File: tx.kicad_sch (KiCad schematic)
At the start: 58 parts, among them Q301 MMBF170, Q302 MMBF170, Q303 MMBF170, Q304 MMBF170, Q305 MMBF170, Q306 MMBF170, Q307 MMBF170, Q308 MMBF170, Q309 MMBF170, Q310 MMBF170, Q311 MMBF170, Q312 MMBF170, T301 BN-43-202_DualPri_CTSec, U301 ICE40UP5K-SG48ITR, U302 CD74ACT541SM96, U303 TLV70012

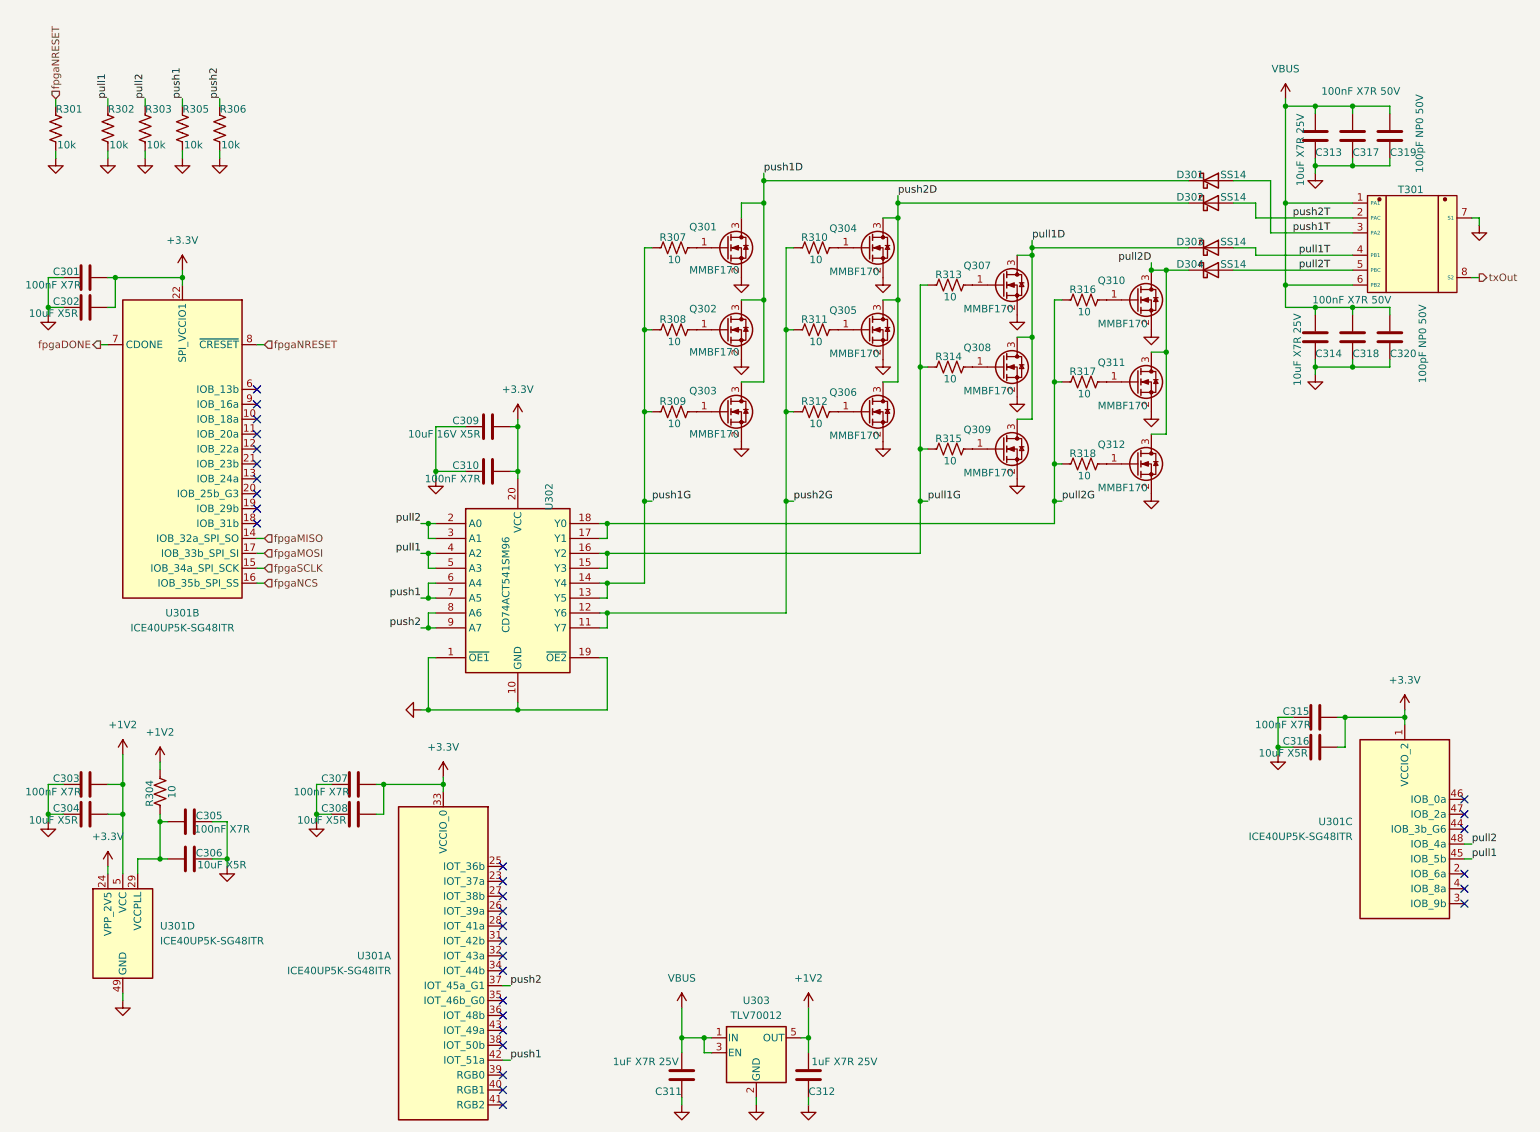
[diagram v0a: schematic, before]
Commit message: Tarted up, 3d models applied, better footprints and BOM, ready to submit for PCBA
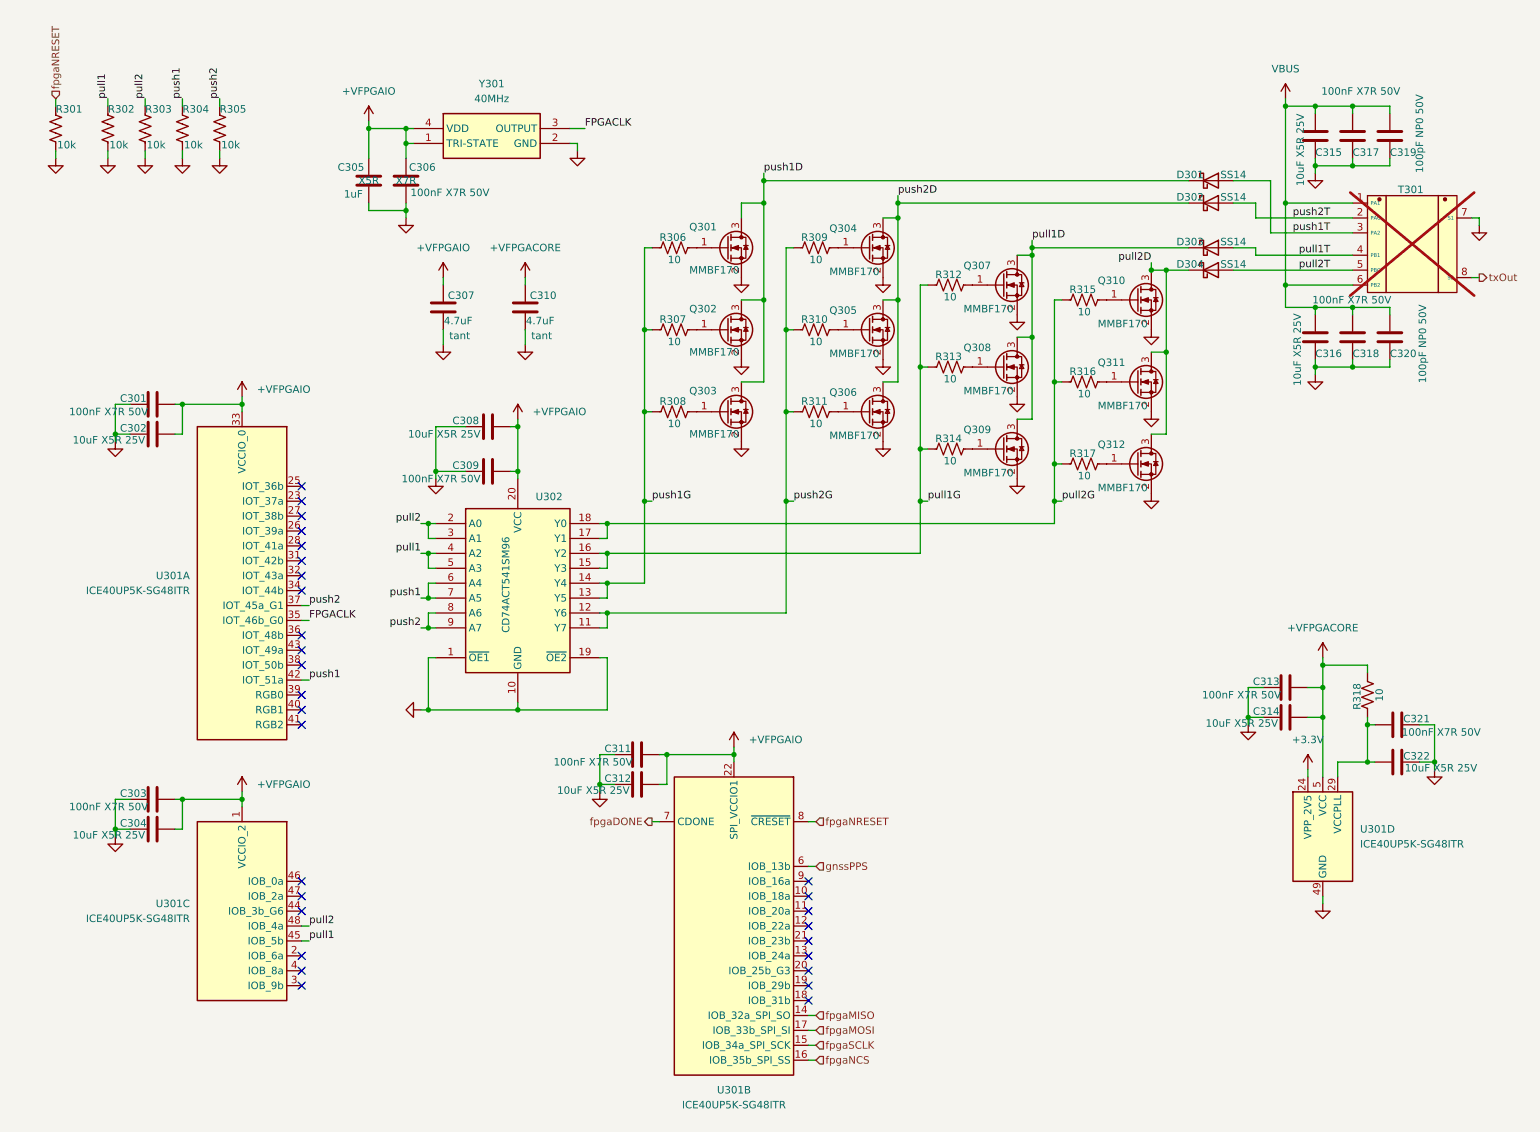
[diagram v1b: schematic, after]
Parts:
- removed C311, C312: 1uF X7R 25V, Capacitor_SMD:C_0603_1608Metric, symbol Device:C
- removed U303: TLV70012, Package_TO_SOT_SMD:SOT-353_SC-70-5, symbol Regulator_Linear:TLV70012_SOT353
- added C305: 1uF, Capacitor_SMD:C_0402_1005Metric, symbol Device:C
- added C306: 100nF X7R 50V, Capacitor_SMD:C_0603_1608Metric, symbol Device:C
- added C307, C310: 4.7uF, Capacitor_SMD:C_0402_1005Metric, symbol Device:C
- added Y301: 40MHz, Library:ECSTXO201633400TR, symbol Library:ECS-TXO-2016-33-400-TR
- C301: renamed from C307; value 100nF X7R -> 100nF X7R 50V; LCSC C14663 -> C24452
- C302: renamed from C308; value 10uF X5R -> 10uF X5R 25V; LCSC C19702 -> C96446
- C303: renamed from C315; value 100nF X7R -> 100nF X7R 50V; LCSC C14663 -> C24452
- C304: renamed from C316; value 10uF X5R -> 10uF X5R 25V; LCSC C19702 -> C96446
- C308: renamed from C309; value 10uF 16V X5R -> 10uF X5R 25V; footprint Capacitor_SMD:C_0805_2012Metric -> Capacitor_SMD:C_0603_1608Metric; LCSC C1713 -> C96446
- C309: renamed from C310; value 100nF X7R -> 100nF X7R 50V; LCSC C14663 -> C24452
- C311: renamed from C301; value 100nF X7R -> 100nF X7R 50V; LCSC C14663 -> C24452
- C312: renamed from C302; value 10uF X5R -> 10uF X5R 25V; LCSC C19702 -> C96446
- C313: renamed from C303; value 100nF X7R -> 100nF X7R 50V; LCSC C14663 -> C24452
- C314: renamed from C304; value 10uF X5R -> 10uF X5R 25V; LCSC C19702 -> C96446
- C315: renamed from C313; value 10uF X7R 25V -> 10uF X5R 25V
- C316: renamed from C314; value 10uF X7R 25V -> 10uF X5R 25V
- C317, C318: LCSC C14663 -> C24452
- C319, C320: footprint Capacitor_SMD:C_0603_1608Metric -> Capacitor_SMD:C_0402_1005Metric; LCSC C14665 -> C106200
- C321: renamed from C305; value 100nF X7R -> 100nF X7R 50V; LCSC C14663 -> C24452
- C322: renamed from C306; value 10uF X5R -> 10uF X5R 25V; LCSC C19702 -> C96446
- R301, R302, R303: footprint Resistor_SMD:R_0603_1608Metric -> Resistor_SMD:R_0402_1005Metric; LCSC C2930027 -> C60490
- R304: renamed from R305; footprint Resistor_SMD:R_0603_1608Metric -> Resistor_SMD:R_0402_1005Metric; LCSC C2930027 -> C60490
- R305: renamed from R306; footprint Resistor_SMD:R_0603_1608Metric -> Resistor_SMD:R_0402_1005Metric; LCSC C2930027 -> C60490
- T301: now not fitted
- renumbered R307 to R306, R308 to R307, R309 to R308, R310 to R309, R311 to R310, R312 to R311, R313 to R312, R314 to R313, R315 to R314, R316 to R315, R317 to R316, R318 to R317, R304 to R318
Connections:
- net +3.3V: no longer C301.2, C302.2, C303.2, C304.2, C308.2, C309.2, C311.2, C312.2, U301.1 (VCCIO_2), U301.22 (SPI_VCCIO1), U301.33 (VCCIO_0), U302.20 (VCC)
- net GND: now also C305.2, C306.2, C307.2, C310.2, Y301.2 (GND)
- net FPGACLK: now reaches U301.35 (IOT_46b_G0)
- net FPGACLK: now also Y301.3 (OUTPUT)
- net gnssPPS: now reaches U301.6 (IOB_13b)
- net +1V2 renamed +VFPGACORE
- net +VFPGACORE: now also C310.1
- new net +VFPGAIO: C301.2, C302.2, C303.2, C304.2, C305.1, C306.1, C307.1, C308.2, C309.2, C311.2, C312.2, U301.1 (VCCIO_2), U301.22 (SPI_VCCIO1), U301.33 (VCCIO_0), U302.20 (VCC), Y301.1 (TRI-STATE), Y301.4 (VDD)
- no-connect marks 31 -> 29
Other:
- moved on the sheet: C301, C302, C303, C304, C311, C312, C313, C314, C321, C322, R318, U301A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
